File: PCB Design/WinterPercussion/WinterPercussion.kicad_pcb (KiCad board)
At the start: 2 copper layers, 55.9 x 59 mm, 6 parts, among them J1 SDS-50J, U1 H11L1M, U2 ESP32-DevKitC

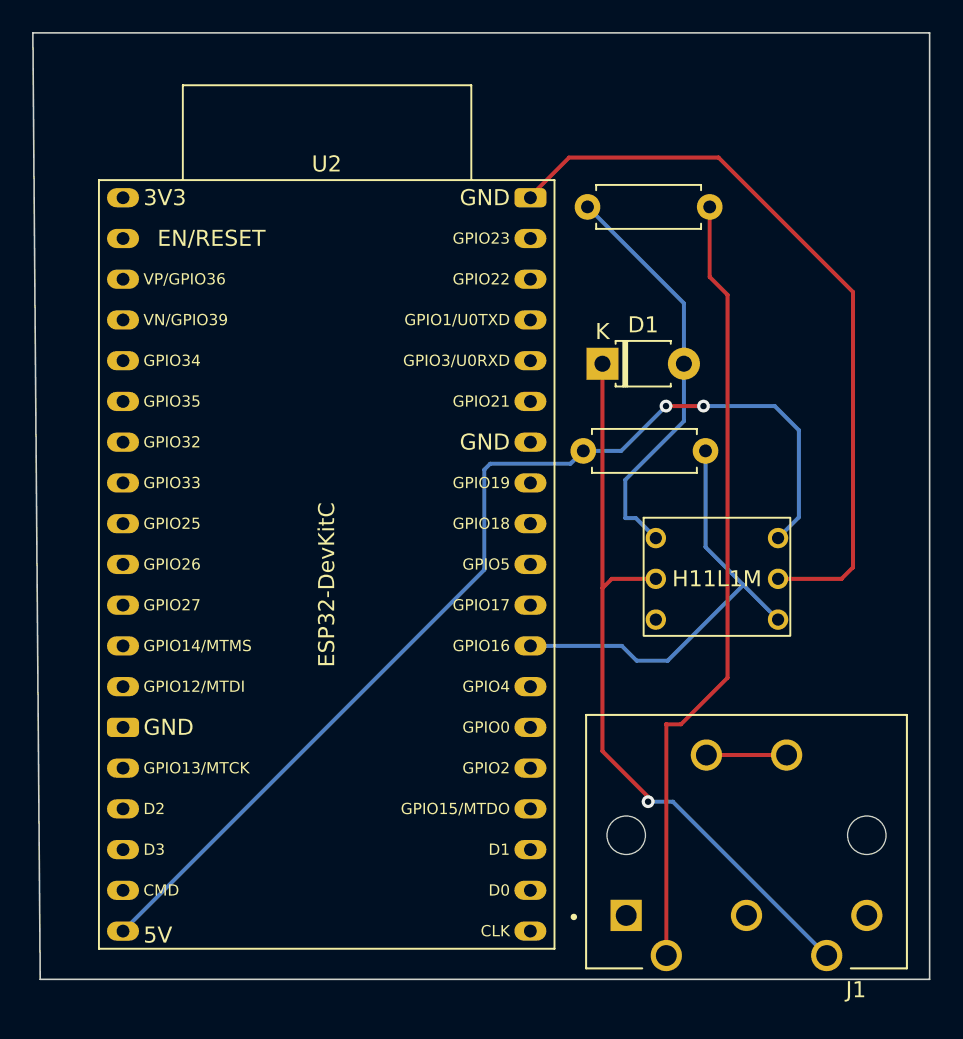
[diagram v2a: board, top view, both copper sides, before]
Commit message: Changed to 3.3v
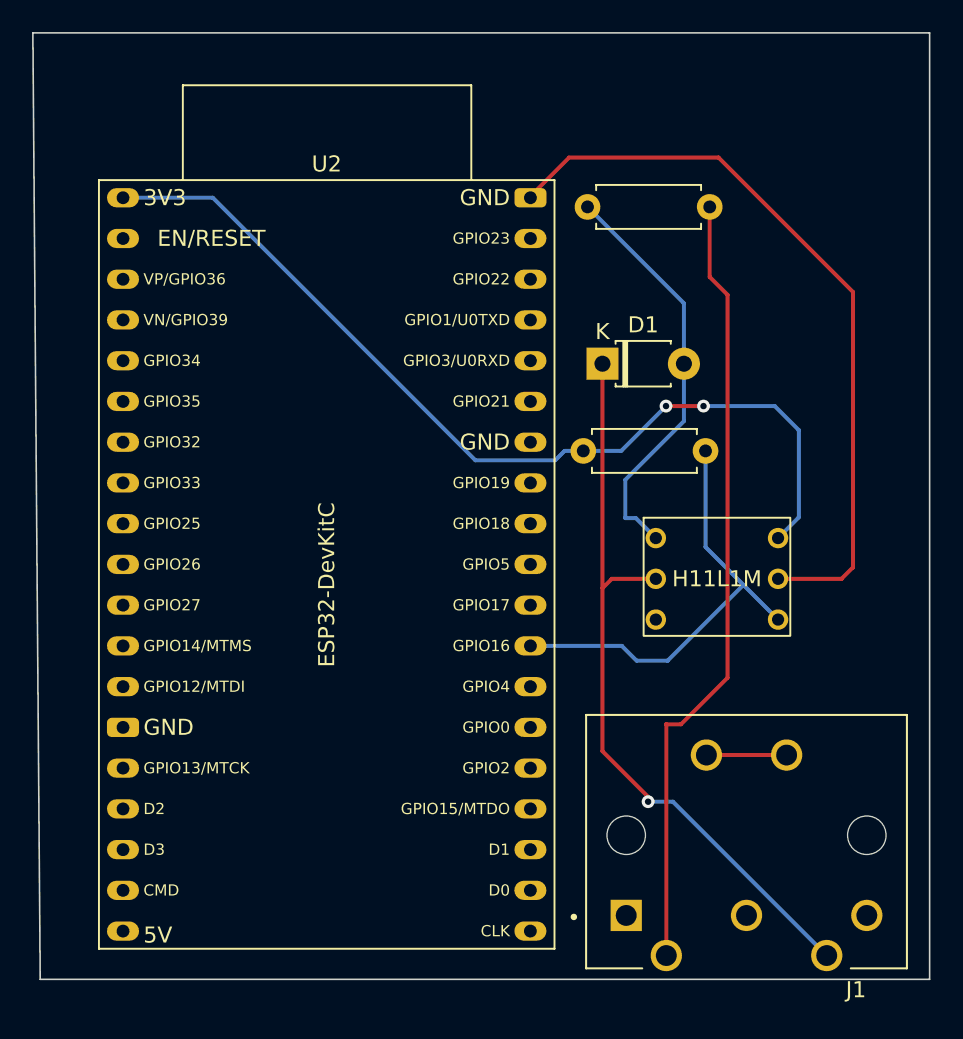
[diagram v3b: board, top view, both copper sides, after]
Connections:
- R2 pad 1: +5V -> +3V3
- U1 pad 6: +5V -> +3V3
- U2 pad 1: unconnected-(U2-Pad1) -> +3V3
- U2 pad 19: +5V -> unconnected-(U2-Pad19)
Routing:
- net +5V: track 67.2 -> 0.00 mm, vias 2 -> 0
- net +3V3: track 0.00 -> 58.2 mm, vias 0 -> 2
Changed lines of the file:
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@@
   (net 8 "unconnected-(U1-Pad3)")
   (net 9 "GND")
-  (net 10 "+5V")
+  (net 10 "+3V3")
   (net 11 "ESP_PIN")
-  (net 12 "unconnected-(U2-Pad1)")
+  (net 12 "unconnected-(U2-Pad19)")
   (net 13 "unconnected-(U2-Pad2)")
   (net 14 "unconnected-(U2-Pad3)")
@@
     )
     (fp_line (start 6.5 -8.3) (end 10 -8.3) (layer "F.SilkS") (width 0.127))
-    (fp_line (start -10 -8.3) (end -6.5 -8.3) (layer "F.SilkS") (width 0.127))
     (fp_line (start 10 -8.3) (end 10 7.5) (layer "F.SilkS") (width 0.127))
     (fp_line (start -10 7.5) (end -10 -8.3) (layer "F.SilkS") (width 0.127))
+    (fp_line (start -10 -8.3) (end -6.5 -8.3) (layer "F.SilkS") (width 0.127))
     (fp_line (start -10 7.5) (end 10 7.5) (layer "F.SilkS") (width 0.127))
     (fp_circle (center 10.764 -5.094) (end 10.864 -5.094) (layer "F.SilkS") (width 0.2) (fill none))
+    (fp_line (start 10.25 -8.55) (end 10.25 7.75) (layer "F.CrtYd") (width 0.05))
+    (fp_line (start 10.25 7.75) (end -10.25 7.75) (layer "F.CrtYd") (width 0.05))
     (fp_line (start -6.25 -8.75) (end 6.25 -8.75) (layer "F.CrtYd") (width 0.05))
+    (fp_line (start -6.25 -8.55) (end -6.25 -8.75) (layer "F.CrtYd") (width 0.05))
+    (fp_line (start -10.25 -8.55) (end -6.25 -8.55) (layer "F.CrtYd") (width 0.05))
     (fp_line (start 6.25 -8.55) (end 10.25 -8.55) (layer "F.CrtYd") (width 0.05))
     (fp_line (start -10.25 7.75) (end -10.25 -8.55) (layer "F.CrtYd") (width 0.05))
-    (fp_line (start 10.25 7.75) (end -10.25 7.75) (layer "F.CrtYd") (width 0.05))
-    (fp_line (start 10.25 -8.55) (end 10.25 7.75) (layer "F.CrtYd") (width 0.05))
-    (fp_line (start -10.25 -8.55) (end -6.25 -8.55) (layer "F.CrtYd") (width 0.05))
-    (fp_line (start -6.25 -8.55) (end -6.25 -8.75) (layer "F.CrtYd") (width 0.05))
     (fp_line (start 6.25 -8.75) (end 6.25 -8.55) (layer "F.CrtYd") (width 0.05))
+    (fp_line (start -10 7.5) (end -10 -8.3) (layer "F.Fab") (width 0.127))
     (fp_line (start -10 -8.3) (end 10 -8.3) (layer "F.Fab") (width 0.127))
     (fp_line (start 10 7.5) (end -10 7.5) (layer "F.Fab") (width 0.127))
     (fp_line (start 10 -8.3) (end 10 7.5) (layer "F.Fab") (width 0.127))
-    (fp_line (start -10 7.5) (end -10 -8.3) (layer "F.Fab") (width 0.127))
     (fp_circle (center 10.764 -5.094) (end 10.864 -5.094) (layer "F.Fab") (width 0.2) (fill none))
     (pad "" np_thru_hole circle (at -7.5 0 180) (size 2.4 2.4) (drill 2.4) (layers *.Cu *.Mask))
@@
     (fp_line (start 6.96 1.25) (end 6.96 -1.25) (layer "F.Fab") (width 0.1))
     (pad "1" thru_hole circle (at 0 0) (size 1.6 1.6) (drill 0.8) (layers *.Cu *.Mask)
-      (net 10 "+5V") (pintype "passive"))
+      (net 10 "+3V3") (pintype "passive"))
     (pad "2" thru_hole oval (at 7.62 0) (size 1.6 1.6) (drill 0.8) (layers *.Cu *.Mask)
       (net 11 "ESP_PIN") (pintype "passive"))
@@
       (net 9 "GND") (pinfunction "GND") (pintype "power_in"))
     (pad "6" thru_hole circle (at 7.62 0) (size 1.27 1.27) (drill 0.762) (layers *.Cu *.Mask)
-      (net 10 "+5V") (pinfunction "VCC") (pintype "power_in"))
+      (net 10 "+3V3") (pinfunction "VCC") (pintype "power_in"))
   )
   (footprint "Espressif:ESP32-DevKitC" (layer "F.Cu")
@@
     (fp_line (start -1.24632 -0.84728) (end 26.65368 -0.84728) (layer "F.CrtYd") (width 0.05))
     (pad "1" thru_hole oval (at 0.00368 0.00272 270) (size 1.2 2) (drill 0.8) (layers *.Cu *.Mask)
-      (net 12 "unconnected-(U2-Pad1)") (pinfunction "3V3") (pintype "power_in+no_connect"))
+      (net 10 "+3V3") (pinfunction "3V3") (pintype "power_in"))
     (pad "2" thru_hole oval (at 0.00368 2.54272 270) (size 1.2 2) (drill 0.8) (layers *.Cu *.Mask)
       (net 13 "unconnected-(U2-Pad2)") (pinfunction "CHIP_PU") (pintype "input+no_connect"))
@@
       (net 29 "unconnected-(U2-Pad18)") (pinfunction "CMD") (pintype "bidirectional+no_connect"))
     (pad "19" thru_hole oval (at 0.00368 45.72272 270) (size 1.2 2) (drill 0.8) (layers *.Cu *.Mask)
-      (net 10 "+5V") (pinfunction "5V") (pintype "power_in"))
+      (net 12 "unconnected-(U2-Pad19)") (pinfunction "5V") (pintype "power_in+no_connect"))
     (pad "20" thru_hole oval (at 25.4 45.72 270) (size 1.2 2) (drill 0.8) (layers *.Cu *.Mask)
       (net 30 "unconnected-(U2-Pad20)") (pinfunction "SD_CLK/GPIO6") (pintype "bidirectional+no_connect"))
@@
   (via (at 141.097 73.8378) (size 0.8) (drill 0.4) (layers "F.Cu" "B.Cu") (net 10))
   (via (at 143.4338 73.8378) (size 0.8) (drill 0.4) (layers "F.Cu" "B.Cu") (net 10))
+  (segment (start 129.2098 77.216) (end 134.1882 77.216) (width 0.25) (layer "B.Cu") (net 10))
   (segment (start 138.303 76.6318) (end 141.097 73.8378) (width 0.25) (layer "B.Cu") (net 10))
-  (segment (start 107.2444 106.56892) (end 129.7686 84.04472) (width 0.25) (layer "B.Cu") (net 10))
   (segment (start 149.3774 75.3364) (end 149.3774 80.772) (width 0.25) (layer "B.Cu") (net 10))
   (segment (start 149.3774 80.772) (end 148.082 82.0674) (width 0.25) (layer "B.Cu") (net 10))
   (segment (start 135.93961 76.6318) (end 138.303 76.6318) (width 0.25) (layer "B.Cu") (net 10))
-  (segment (start 135.139611 77.431799) (end 135.93961 76.6318) (width 0.25) (layer "B.Cu") (net 10))
-  (segment (start 130.137001 77.431799) (end 135.139611 77.431799) (width 0.25) (layer "B.Cu") (net 10))
-  (segment (start 129.7686 77.8002) (end 130.137001 77.431799) (width 0.25) (layer "B.Cu") (net 10))
+  (segment (start 134.7724 76.6318) (end 135.93961 76.6318) (width 0.25) (layer "B.Cu") (net 10))
+  (segment (start 107.2444 60.84892) (end 112.84272 60.84892) (width 0.25) (layer "B.Cu") (net 10))
+  (segment (start 112.84272 60.84892) (end 129.2098 77.216) (width 0.25) (layer "B.Cu") (net 10))
   (segment (start 147.8788 73.8378) (end 149.3774 75.3364) (width 0.25) (layer "B.Cu") (net 10))
   (segment (start 143.4338 73.8378) (end 147.8788 73.8378) (width 0.25) (layer "B.Cu") (net 10))
-  (segment (start 129.7686 84.04472) (end 129.7686 77.8002) (width 0.25) (layer "B.Cu") (net 10))
+  (segment (start 134.1882 77.216) (end 134.7724 76.6318) (width 0.25) (layer "B.Cu") (net 10))
   (segment (start 145.923 84.9884) (end 148.082 87.1474) (width 0.25) (layer "B.Cu") (net 11))
   (segment (start 138.34432 88.78892) (end 139.2682 89.7128) (width 0.25) (layer "B.Cu") (net 11))
